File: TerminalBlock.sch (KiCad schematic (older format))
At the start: 2 parts, among them P4 12-pin Terminal Block, P5 3-pin TB

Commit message: Updates from Layout Work Session 5 video
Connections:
- net GND renamed GND_PWR
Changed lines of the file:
@@
 RELAY_NC
 $Comp
-L +3.3V #PWR021
+L +3.3V #PWR022
 U 1 1 52FC1D46
 P 1900 2950
-F 0 "#PWR021" H 1900 2910 30  0001 C CNN
+F 0 "#PWR022" H 1900 2910 30  0001 C CNN
 F 1 "+3.3V" H 1900 3060 30  0000 C CNN
 F 2 "" H 1900 2950 60  0000 C CNN
@@
 $EndComp
 $Comp
-L +5V #PWR022
+L +5V #PWR023
 U 1 1 52FC1D5A
 P 1700 2950
-F 0 "#PWR022" H 1700 3040 20  0001 C CNN
+F 0 "#PWR023" H 1700 3040 20  0001 C CNN
 F 1 "+5V" H 1700 3040 30  0000 C CNN
 F 2 "" H 1700 2950 60  0000 C CNN
 F 3 "" H 1700 2950 60  0000 C CNN
 	1    1700 2950
-	1    0    0    -1
-$EndComp
-$Comp
-L GND #PWR023
-U 1 1 52FC1D6E
-P 2200 2900
-F 0 "#PWR023" H 2200 2900 30  0001 C CNN
-F 1 "GND" H 2200 2830 30  0001 C CNN
-F 2 "" H 2200 2900 60  0000 C CNN
-F 3 "" H 2200 2900 60  0000 C CNN
-	1    2200 2900
 	1    0    0    -1
 $EndComp
@@
 Wire Wire Line
 	2200 2800 2200 2900
+$Comp
+L GND_PWR #PWR024
+U 1 1 53163AD6
+P 2200 2900
+F 0 "#PWR024" H 2200 2900 30  0001 C CNN
+F 1 "GND_PWR" H 2200 2830 30  0000 C CNN
+F 2 "" H 2200 2900 60  0000 C CNN
+F 3 "" H 2200 2900 60  0000 C CNN
+	1    2200 2900
+	1    0    0    -1
+$EndComp
 $EndSCHEMATC

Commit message: Updates from Layout Work Session 6 video
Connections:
- net +3.3V: now also P4.10 (P10); no longer P4.9 (P9)
- net +5V: now also P4.8 (P8); no longer P4.10 (P10)
- net GND_PWR: now also P4.9 (P9); no longer P4.8 (P8)
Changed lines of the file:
@@
 RELAY_NC
 $Comp
-L +3.3V #PWR022
+L +3.3V #PWR025
 U 1 1 52FC1D46
-P 1900 2950
-F 0 "#PWR022" H 1900 2910 30  0001 C CNN
-F 1 "+3.3V" H 1900 3060 30  0000 C CNN
-F 2 "" H 1900 2950 60  0000 C CNN
-F 3 "" H 1900 2950 60  0000 C CNN
-	1    1900 2950
+P 1600 2950
+F 0 "#PWR025" H 1600 2910 30  0001 C CNN
+F 1 "+3.3V" H 1600 3060 30  0000 C CNN
+F 2 "" H 1600 2950 60  0000 C CNN
+F 3 "" H 1600 2950 60  0000 C CNN
+	1    1600 2950
 	1    0    0    -1
 $EndComp
 $Comp
-L +5V #PWR023
+L +5V #PWR026
 U 1 1 52FC1D5A
-P 1700 2950
-F 0 "#PWR023" H 1700 3040 20  0001 C CNN
-F 1 "+5V" H 1700 3040 30  0000 C CNN
-F 2 "" H 1700 2950 60  0000 C CNN
-F 3 "" H 1700 2950 60  0000 C CNN
-	1    1700 2950
+P 2200 2650
+F 0 "#PWR026" H 2200 2740 20  0001 C CNN
+F 1 "+5V" H 2200 2740 30  0000 C CNN
+F 2 "" H 2200 2650 60  0000 C CNN
+F 3 "" H 2200 2650 60  0000 C CNN
+	1    2200 2650
 	1    0    0    -1
 $EndComp
@@
 	3100 2100 4000 2100
 Wire Wire Line
-	3100 3000 3100 2100
+	3100 2850 3100 2100
 Wire Wire Line
-	1900 3000 3100 3000
+	1900 2850 3100 2850
 Wire Wire Line
 	3000 2000 4000 2000
 Wire Wire Line
-	3000 2800 3000 2000
+	3000 2700 3000 2000
 Wire Wire Line
-	2200 2800 3000 2800
+	2200 2700 3000 2700
 Wire Wire Line
 	2800 1900 4000 1900
@@
 	2500 2000 2500 1700
 Wire Wire Line
-	1700 3100 3200 3100
+	1600 3100 3200 3100
 Wire Wire Line
 	2400 1600 4000 1600
@@
 	2200 1300 4000 1300
 Wire Wire Line
-	1900 2950 1900 3000
+	2200 2650 2200 2700
 Wire Wire Line
 	3200 3100 3200 2200
@@
 	3550 4000 4000 4000
 Wire Wire Line
-	1700 2950 1700 3100
+	1600 2950 1600 3100
 Wire Wire Line
 	2200 2400 2800 2400
@@
 	2300 1800 2200 1800
 Wire Wire Line
-	2200 2800 2200 2900
+	1900 2850 1900 2950
 $Comp
-L GND_PWR #PWR024
+L GND_PWR #PWR027
 U 1 1 53163AD6
-P 2200 2900
-F 0 "#PWR024" H 2200 2900 30  0001 C CNN
-F 1 "GND_PWR" H 2200 2830 30  0000 C CNN
-F 2 "" H 2200 2900 60  0000 C CNN
-F 3 "" H 2200 2900 60  0000 C CNN
-	1    2200 2900
+P 1900 2950
+F 0 "#PWR027" H 1900 2950 30  0001 C CNN
+F 1 "GND_PWR" H 1900 2880 30  0000 C CNN
+F 2 "" H 1900 2950 60  0000 C CNN
+F 3 "" H 1900 2950 60  0000 C CNN
+	1    1900 2950
 	1    0    0    -1
 $EndComp

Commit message: Updates from Layout Work Session 7 video
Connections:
- net +5V renamed +5P
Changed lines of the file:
@@
 RELAY_NC
 $Comp
-L +3.3V #PWR025
+L +3.3V #PWR28
 U 1 1 52FC1D46
 P 1600 2950
-F 0 "#PWR025" H 1600 2910 30  0001 C CNN
+F 0 "#PWR28" H 1600 2910 30  0001 C CNN
 F 1 "+3.3V" H 1600 3060 30  0000 C CNN
 F 2 "" H 1600 2950 60  0000 C CNN
 F 3 "" H 1600 2950 60  0000 C CNN
 	1    1600 2950
-	1    0    0    -1
-$EndComp
-$Comp
-L +5V #PWR026
-U 1 1 52FC1D5A
-P 2200 2650
-F 0 "#PWR026" H 2200 2740 20  0001 C CNN
-F 1 "+5V" H 2200 2740 30  0000 C CNN
-F 2 "" H 2200 2650 60  0000 C CNN
-F 3 "" H 2200 2650 60  0000 C CNN
-	1    2200 2650
 	1    0    0    -1
 $EndComp
@@
 	1900 2850 1900 2950
 $Comp
-L GND_PWR #PWR027
+L GND_PWR #PWR29
 U 1 1 53163AD6
 P 1900 2950
-F 0 "#PWR027" H 1900 2950 30  0001 C CNN
+F 0 "#PWR29" H 1900 2950 30  0001 C CNN
 F 1 "GND_PWR" H 1900 2880 30  0000 C CNN
 F 2 "" H 1900 2950 60  0000 C CNN
@@
 	1    0    0    -1
 $EndComp
+$Comp
+L +5P #PWR30
+U 1 1 531668FE
+P 2200 2650
+F 0 "#PWR30" H 2200 2780 20  0001 C CNN
+F 1 "+5P" H 2200 2750 30  0000 C CNN
+F 2 "" H 2200 2650 60  0000 C CNN
+F 3 "" H 2200 2650 60  0000 C CNN
+	1    2200 2650
+	1    0    0    -1
+$EndComp

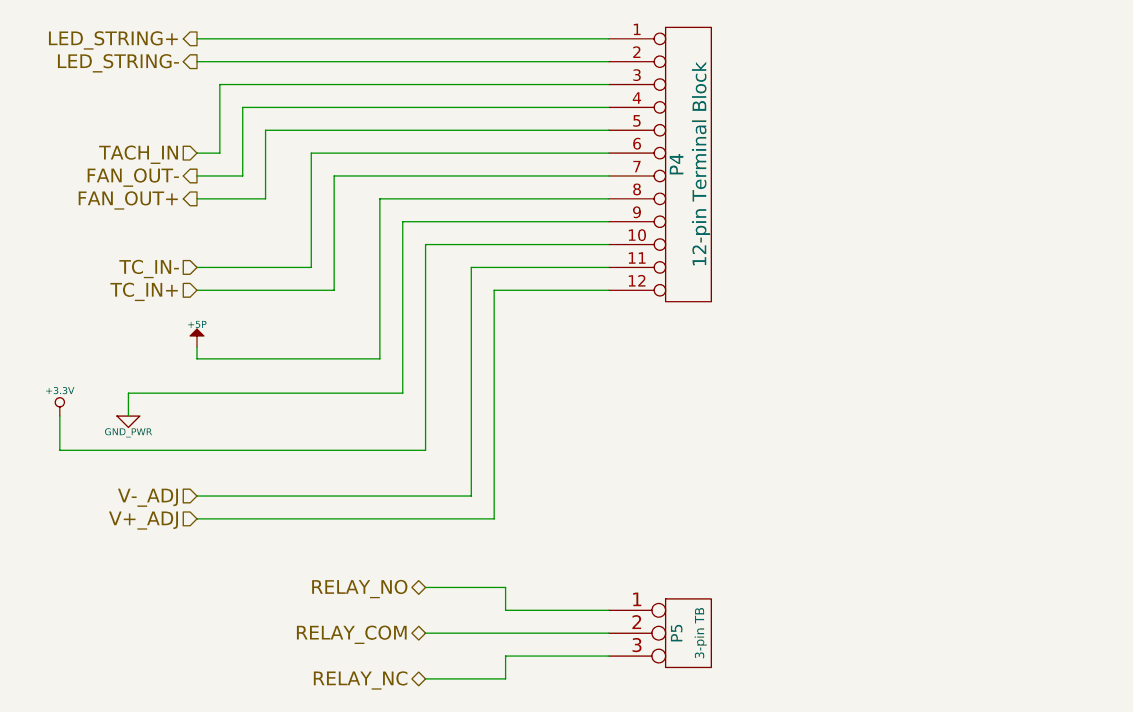
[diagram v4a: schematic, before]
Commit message: Connected remaing nets
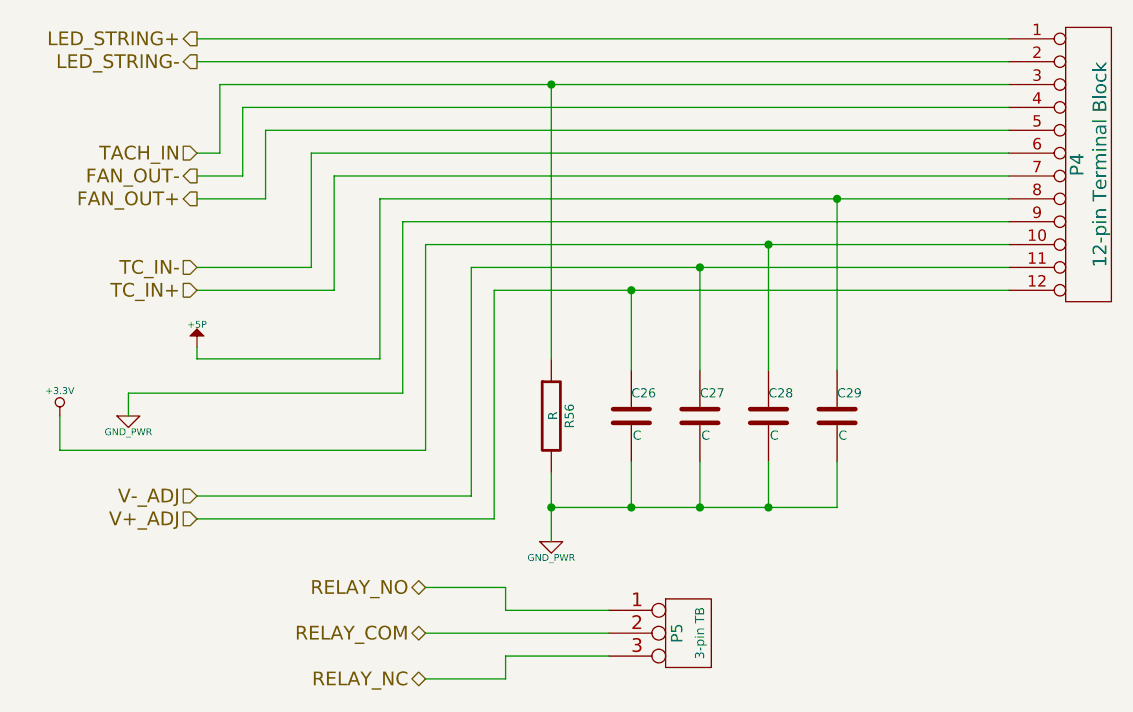
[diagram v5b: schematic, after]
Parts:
- added C26, C27, C28, C29: C, symbol C
- added R56: R, symbol R
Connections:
- net +3.3V: now also C28.1
- net +5P: now also C29.1
- net GND_PWR: now also C26.2, C27.2, C28.2, C29.2, R56.2
- net TACH_IN: now also R56.1
- net V+_ADJ: now also C26.1
- net V-_ADJ: now also C27.1
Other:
- moved on the sheet: P4
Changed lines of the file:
@@
 RELAY_NC
 $Comp
-L +3.3V #PWR025
+L +3.3V #PWR28
 U 1 1 52FC1D46
 P 1600 2950
-F 0 "#PWR025" H 1600 2910 30  0001 C CNN
+F 0 "#PWR28" H 1600 2910 30  0001 C CNN
 F 1 "+3.3V" H 1600 3060 30  0000 C CNN
 F 2 "" H 1600 2950 60  0000 C CNN
@@
 L CONN_12 P4
 U 1 1 5308C0F9
-P 4350 1850
-F 0 "P4" V 4300 1850 60  0000 C CNN
-F 1 "12-pin Terminal Block" V 4400 1850 60  0000 C CNN
-F 2 "" H 4350 1850 60  0000 C CNN
-F 3 "" H 4350 1850 60  0000 C CNN
-F 4 "On Shore" H 4350 1850 60  0001 C CNN "MFG Name"
-F 5 "OSTTE120104" H 4350 1850 60  0001 C CNN "MFG Part Number"
-	1    4350 1850
+P 6100 1850
+F 0 "P4" V 6050 1850 60  0000 C CNN
+F 1 "12-pin Terminal Block" V 6150 1850 60  0000 C CNN
+F 2 "" H 6100 1850 60  0000 C CNN
+F 3 "" H 6100 1850 60  0000 C CNN
+F 4 "On Shore" H 6100 1850 60  0001 C CNN "MFG Name"
+F 5 "OSTTE120104" H 6100 1850 60  0001 C CNN "MFG Part Number"
+	1    6100 1850
 	1    0    0    -1
 $EndComp
@@
 $EndComp
 Wire Wire Line
-	3100 2100 4000 2100
+	3100 2100 5750 2100
 Wire Wire Line
 	3100 2850 3100 2100
@@
 	1900 2850 3100 2850
 Wire Wire Line
-	3000 2000 4000 2000
+	3000 2000 5750 2000
 Wire Wire Line
 	3000 2700 3000 2000
@@
 	2200 2700 3000 2700
 Wire Wire Line
-	2800 1900 4000 1900
+	2800 1900 5750 1900
 Wire Wire Line
 	2800 2400 2800 1900
@@
 	2200 2000 2500 2000
 Wire Wire Line
-	2700 1800 4000 1800
+	2700 1800 5750 1800
 Wire Wire Line
 	2200 1900 2400 1900
 Wire Wire Line
-	2500 1700 4000 1700
+	2500 1700 5750 1700
 Wire Wire Line
 	2500 2000 2500 1700
@@
 	1600 3100 3200 3100
 Wire Wire Line
-	2400 1600 4000 1600
+	2400 1600 5750 1600
 Wire Wire Line
 	2400 1900 2400 1600
 Wire Wire Line
-	2300 1500 4000 1500
+	2300 1500 5750 1500
 Wire Wire Line
 	2300 1500 2300 1800
 Wire Wire Line
-	2200 1400 4000 1400
-Wire Wire Line
-	2200 1300 4000 1300
+	2200 1400 5750 1400
+Wire Wire Line
+	2200 1300 5750 1300
 Wire Wire Line
 	2200 2650 2200 2700
@@
 	3200 3100 3200 2200
 Wire Wire Line
-	3200 2200 4000 2200
+	3200 2200 5750 2200
 Wire Wire Line
 	2200 3300 3400 3300
@@
 	3400 3300 3400 2300
 Wire Wire Line
-	3400 2300 4000 2300
+	3400 2300 5750 2300
 Wire Wire Line
 	2200 3400 3500 3400
@@
 	3500 3400 3500 2400
 Wire Wire Line
-	3500 2400 4000 2400
+	3500 2400 5750 2400
 Wire Wire Line
 	4000 3800 3550 3800
@@
 	1900 2850 1900 2950
 $Comp
-L GND_PWR #PWR026
+L GND_PWR #PWR29
 U 1 1 53163AD6
 P 1900 2950
-F 0 "#PWR026" H 1900 2950 30  0001 C CNN
+F 0 "#PWR29" H 1900 2950 30  0001 C CNN
 F 1 "GND_PWR" H 1900 2880 30  0000 C CNN
 F 2 "" H 1900 2950 60  0000 C CNN
@@
 	1    0    0    -1
 $EndComp
+$Comp
+L R R56
+U 1 1 531F9C44
+P 3750 2950
+F 0 "R56" V 3830 2950 40  0000 C CNN
+F 1 "R" V 3757 2951 40  0000 C CNN
+F 2 "" V 3680 2950 30  0000 C CNN
+F 3 "" H 3750 2950 30  0000 C CNN
+	1    3750 2950
+	1    0    0    -1
+$EndComp
+Wire Wire Line
+	3750 3200 3750 3500
+$Comp
+L GND_PWR #PWR31
+U 1 1 531F9C57
+P 3750 3500
+F 0 "#PWR31" H 3750 3500 30  0001 C CNN
+F 1 "GND_PWR" H 3750 3430 30  0000 C CNN
+F 2 "" H 3750 3500 60  0000 C CNN
+F 3 "" H 3750 3500 60  0000 C CNN
+	1    3750 3500
+	1    0    0    -1
+$EndComp
+Wire Wire Line
+	3750 2700 3750 1500
+Connection ~ 3750 1500
+$Comp
+L C C26
+U 1 1 531FA44D
+P 4100 2950
+F 0 "C26" H 4100 3050 40  0000 L CNN
+F 1 "C" H 4106 2865 40  0000 L CNN
+F 2 "" H 4138 2800 30  0000 C CNN
+F 3 "" H 4100 2950 60  0000 C CNN
+	1    4100 2950
+	1    0    0    -1
+$EndComp
+Wire Wire Line
+	3750 3350 5000 3350
+Wire Wire Line
+	4100 3350 4100 3150
+Connection ~ 3750 3350
+$Comp
+L C C27
+U 1 1 531FA49F
+P 4400 2950
+F 0 "C27" H 4400 3050 40  0000 L CNN
+F 1 "C" H 4406 2865 40  0000 L CNN
+F 2 "" H 4438 2800 30  0000 C CNN
+F 3 "" H 4400 2950 60  0000 C CNN
+	1    4400 2950
+	1    0    0    -1
+$EndComp
+Wire Wire Line
+	4400 3350 4400 3150
+Connection ~ 4100 3350
+$Comp
+L C C28
+U 1 1 531FA4DD
+P 4700 2950
+F 0 "C28" H 4700 3050 40  0000 L CNN
+F 1 "C" H 4706 2865 40  0000 L CNN
+F 2 "" H 4738 2800 30  0000 C CNN
+F 3 "" H 4700 2950 60  0000 C CNN
+	1    4700 2950
+	1    0    0    -1
+$EndComp
+Wire Wire Line
+	4700 3350 4700 3150
+$Comp
+L C C29
+U 1 1 531FA4E4
+P 5000 2950
+F 0 "C29" H 5000 3050 40  0000 L CNN
+F 1 "C" H 5006 2865 40  0000 L CNN
+F 2 "" H 5038 2800 30  0000 C CNN
+F 3 "" H 5000 2950 60  0000 C CNN
+	1    5000 2950
+	1    0    0    -1
+$EndComp
+Wire Wire Line
+	5000 3350 5000 3150
+Connection ~ 4400 3350
+Connection ~ 4700 3350
+Wire Wire Line
+	4100 2750 4100 2400
+Connection ~ 4100 2400
+Wire Wire Line
+	4400 2750 4400 2300
+Connection ~ 4400 2300
+Wire Wire Line
+	4700 2750 4700 2200
+Connection ~ 4700 2200
+Wire Wire Line
+	5000 2750 5000 2000
+Connection ~ 5000 2000
 $EndSCHEMATC

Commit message: Added some R/C to analog sections
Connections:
- net TC_IN+: now also P4.6 (P6); no longer P4.7 (P7)
- net TC_IN-: now also P4.7 (P7); no longer P4.6 (P6)
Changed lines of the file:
@@
 LED_STRING-
 Text HLabel 2200 2400 0    60   Input ~ 0
+TC_IN-
+Text HLabel 2200 2300 0    60   Input ~ 0
 TC_IN+
-Text HLabel 2200 2300 0    60   Input ~ 0
-TC_IN-
 Text HLabel 3200 3900 0    60   BiDi ~ 0
 RELAY_COM

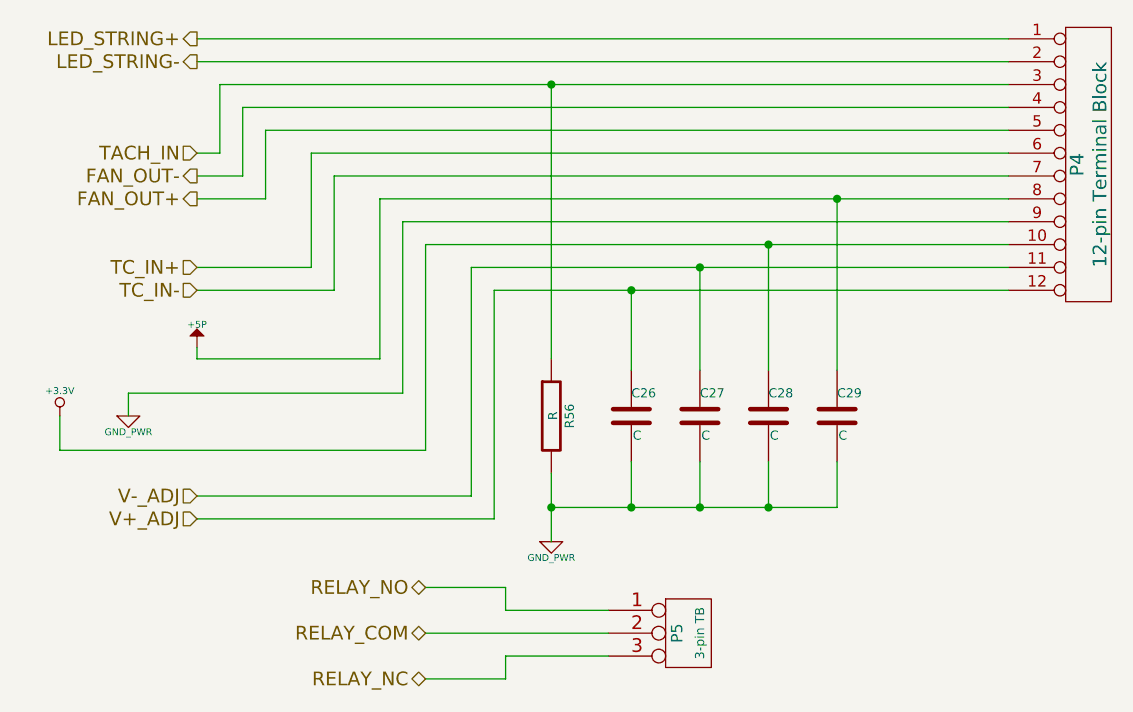
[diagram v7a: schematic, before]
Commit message: Assigned values to passives in Arduino, power adjustment monitor, relay and terminal block schematics
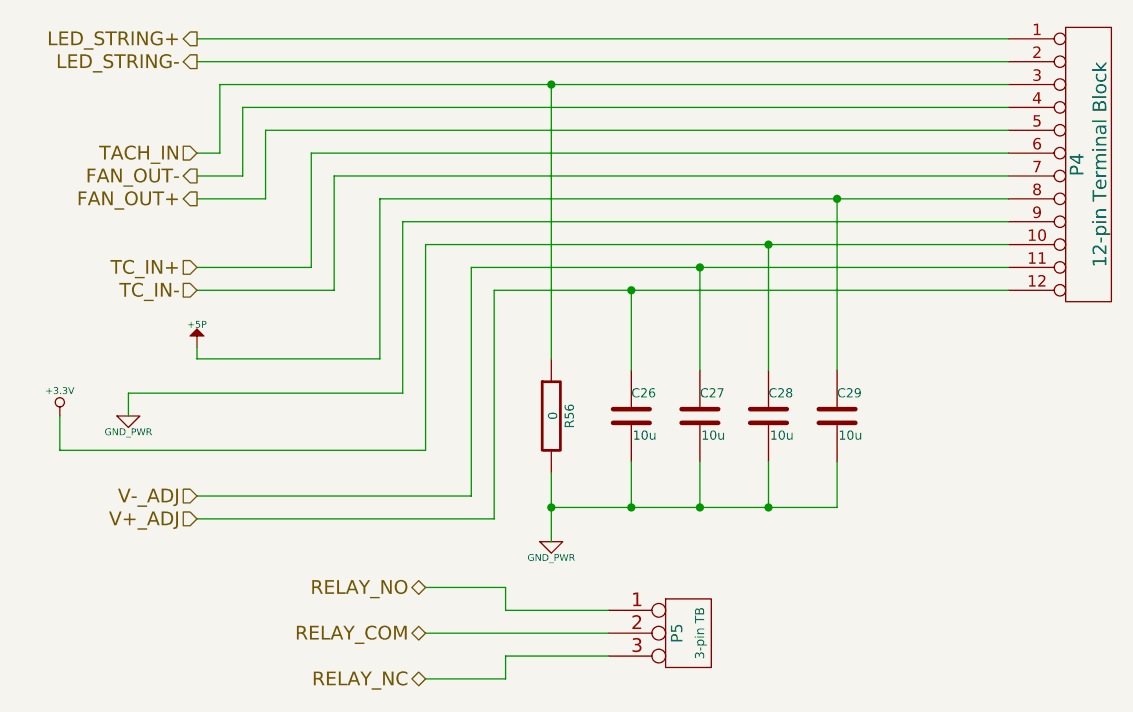
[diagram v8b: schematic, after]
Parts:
- C26, C27, C28, C29: value C -> 10u
- R56: value R -> 0
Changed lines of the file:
@@
 P 3750 2950
 F 0 "R56" V 3830 2950 40  0000 C CNN
-F 1 "R" V 3757 2951 40  0000 C CNN
+F 1 "0" V 3757 2951 40  0000 C CNN
 F 2 "" V 3680 2950 30  0000 C CNN
 F 3 "" H 3750 2950 30  0000 C CNN
@@
 P 4100 2950
 F 0 "C26" H 4100 3050 40  0000 L CNN
-F 1 "C" H 4106 2865 40  0000 L CNN
+F 1 "10u" H 4106 2865 40  0000 L CNN
 F 2 "" H 4138 2800 30  0000 C CNN
 F 3 "" H 4100 2950 60  0000 C CNN
@@
 P 4400 2950
 F 0 "C27" H 4400 3050 40  0000 L CNN
-F 1 "C" H 4406 2865 40  0000 L CNN
+F 1 "10u" H 4406 2865 40  0000 L CNN
 F 2 "" H 4438 2800 30  0000 C CNN
 F 3 "" H 4400 2950 60  0000 C CNN
@@
 P 4700 2950
 F 0 "C28" H 4700 3050 40  0000 L CNN
-F 1 "C" H 4706 2865 40  0000 L CNN
+F 1 "10u" H 4706 2865 40  0000 L CNN
 F 2 "" H 4738 2800 30  0000 C CNN
 F 3 "" H 4700 2950 60  0000 C CNN
@@
 P 5000 2950
 F 0 "C29" H 5000 3050 40  0000 L CNN
-F 1 "C" H 5006 2865 40  0000 L CNN
+F 1 "10u" H 5006 2865 40  0000 L CNN
 F 2 "" H 5038 2800 30  0000 C CNN
 F 3 "" H 5000 2950 60  0000 C CNN
